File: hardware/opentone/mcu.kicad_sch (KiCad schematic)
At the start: 31 parts, among them J401 SWD 2x5 1.27mm, J402 ST-LINK (Nucleo CN4), J403 Log UART4, J404 Spare GPIO, SW401 RESET, SW402 BOOT0 (DFU), U401 STM32F446VETx, Y401 8MHz, Y402 32.768kHz

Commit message: added sd card, haptic, updated old parts and set a datasheet and MPN to all parts
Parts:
- C401, C402, C403, C404, C405, C406, C408, C410, C417: footprint Capacitor_SMD:C_0805_2012Metric -> Capacitor_SMD:C_0603_1608Metric; LCSC (none) -> C14663; Manufacturer (none) -> YAGEO; Part number (none) -> CC0603KRX7R9BB104
- C407: footprint Capacitor_SMD:C_0805_2012Metric -> Capacitor_SMD:C_0603_1608Metric; LCSC (none) -> C19666; Manufacturer (none) -> Samsung Electro-Mechanics; Part number (none) -> CL10A475KO8NNNC
- C409: footprint Capacitor_SMD:C_0805_2012Metric -> Capacitor_SMD:C_0603_1608Metric; LCSC (none) -> C15849; Manufacturer (none) -> Samsung Electro-Mechanics; Part number (none) -> CL10A105KB8NNNC
- C411, C412: footprint Capacitor_SMD:C_0805_2012Metric -> Capacitor_SMD:C_0603_1608Metric; LCSC (none) -> C23630; Manufacturer (none) -> Samsung Electro-Mechanics; Part number (none) -> CL10A225KO8NNNC
- C413, C414: footprint Capacitor_SMD:C_0805_2012Metric -> Capacitor_SMD:C_0603_1608Metric; LCSC (none) -> C1644; Manufacturer (none) -> Samsung Electro-Mechanics; Part number (none) -> CL10C150JB8NNNC
- C415, C416: footprint Capacitor_SMD:C_0805_2012Metric -> Capacitor_SMD:C_0603_1608Metric; LCSC (none) -> C1679; Manufacturer (none) -> FH (Guangdong Fenghua); Part number (none) -> 0603CG6R8C500NT
- FB401: footprint Inductor_SMD:L_0805_2012Metric -> Inductor_SMD:L_0603_1608Metric; LCSC (none) -> C1002; Manufacturer (none) -> Sunlord; Part number (none) -> GZ1608D601TF
- J401: LCSC (none) -> C150517; Manufacturer (none) -> Amphenol ICC; Part number (none) -> 20021121-00010C4LF; now left out of the parts list
- J402, J403, J404, JP401: now left out of the parts list
- R401: footprint Resistor_SMD:R_0805_2012Metric -> Resistor_SMD:R_0603_1608Metric; LCSC (none) -> C25804; Manufacturer (none) -> UNI-ROYAL; Part number (none) -> 0603WAF1002T5E
- R402, R403: footprint Resistor_SMD:R_0805_2012Metric -> Resistor_SMD:R_0603_1608Metric; LCSC (none) -> C23162; Manufacturer (none) -> UNI-ROYAL; Part number (none) -> 0603WAF4701T5E
- SW401, SW402: LCSC (none) -> C221895; Manufacturer (none) -> C&K; Part number (none) -> PTS810SJG250SMTRLFS
- U401: LCSC (none) -> C91929
- Y401: LCSC (none) -> C19076848; Manufacturer (none) -> KYX; Part number (none) -> K3A080001010
- Y402: LCSC (none) -> C20340322; Manufacturer (none) -> Seiko Epson; Part number (none) -> FC-135 32.7680KA-E

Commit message: added recommendations from Teel s checklists
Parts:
- added D401: STATUS, LED_SMD:LED_0603_1608Metric, symbol Device:LED
- added R404: 1k, Resistor_SMD:R_0603_1608Metric, symbol Device:R
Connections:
- net MCU_3V3: now also D401.2 (A)
- net SPARE_PC13 renamed STATUS_LED
- net STATUS_LED: now also R404.2
- new net: D401.1 (K), R404.1

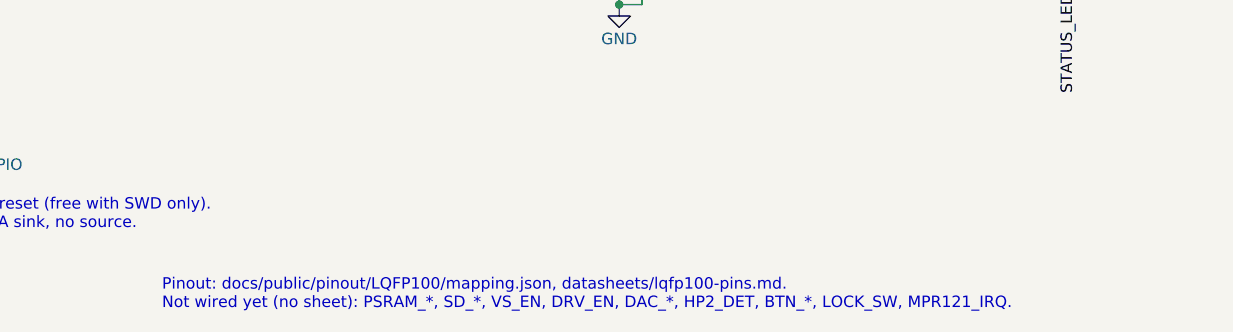
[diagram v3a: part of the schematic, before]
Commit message: license and datasheets script
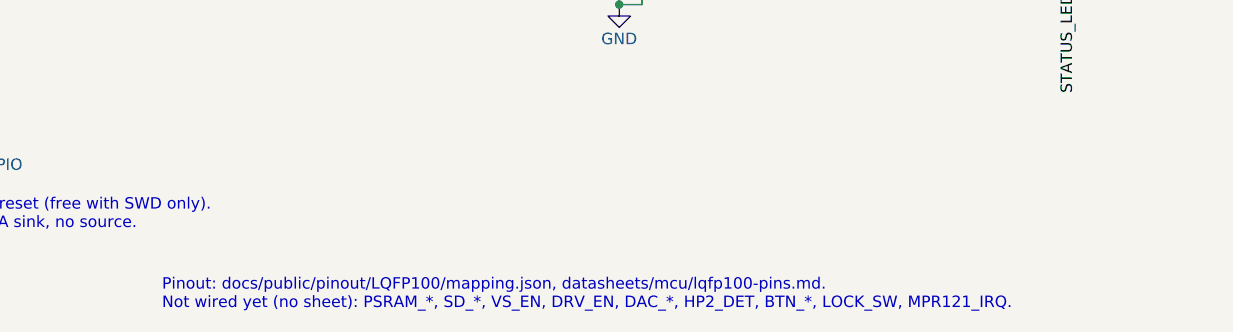
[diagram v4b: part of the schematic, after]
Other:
- note added: "Pinout: docs/public/pinout/LQFP100/mapping.json, datasheets/mcu/lqfp100-pins.md. Not wired yet (no sheet): PSRAM_*, SD_*, VS_EN, DRV_EN, DAC_*, HP2_DET, BTN_*, LOCK_SW, MPR121_IRQ."
- note removed: "Pinout: docs/public/pinout/LQFP100/mapping.json, datasheets/lqfp100-pins.md. Not wired yet (no sheet): PSRAM_*, SD_*, VS_EN, DRV_EN, DAC_*, HP2_DET, BTN_*, LOCK_SW, MPR121_IRQ."
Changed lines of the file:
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@@
 		(comment 1 "STM32F446VET6 (LQFP100), supply, crystals, reset/boot, SWD")
 	)
-	(text "Pinout: docs/public/pinout/LQFP100/mapping.json, datasheets/lqfp100-pins.md.\nNot wired yet (no sheet): PSRAM_*, SD_*, VS_EN, DRV_EN, DAC_*, HP2_DET, BTN_*, LOCK_SW, MPR121_IRQ."
+	(text "Pinout: docs/public/pinout/LQFP100/mapping.json, datasheets/mcu/lqfp100-pins.md.\nNot wired yet (no sheet): PSRAM_*, SD_*, VS_EN, DRV_EN, DAC_*, HP2_DET, BTN_*, LOCK_SW, MPR121_IRQ."
 		(exclude_from_sim no)
 		(at 177.8 248.92 0)

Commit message: DAC
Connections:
- net HP2_DET renamed DAC_INT

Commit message: updated BOM
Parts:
- C401, C402, C403, C404, C405, C406, C408, C410, C417: value 100n -> 100nF
- C407: value 4.7u -> 4.7uF
- C409: value 1u -> 1uF
- C411, C412: value 2.2u -> 2.2uF
- C413, C414: value 15p -> 15pF
- C415, C416: value 6.8p -> 6.8pF
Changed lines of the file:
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@@
 			)
 		)
-		(property "Value" "2.2u"
+		(property "Value" "2.2uF"
 			(at 92.71 71.12 0)
 			(show_name no)
@@
 			)
 		)
-		(property "Value" "1u"
+		(property "Value" "1uF"
 			(at 49.53 71.12 0)
 			(show_name no)
@@
 			)
 		)
-		(property "Value" "6.8p"
+		(property "Value" "6.8pF"
 			(at 120.65 104.14 0)
 			(show_name no)
@@
 			)
 		)
-		(property "Value" "100n"
+		(property "Value" "100nF"
 			(at 85.09 40.64 0)
 			(show_name no)
@@
 			)
 		)
-		(property "Value" "100n"
+		(property "Value" "100nF"
 			(at 59.69 71.12 0)
 			(show_name no)
@@
 			)
 		)
-		(property "Value" "100n"
+		(property "Value" "100nF"
 			(at 105.41 40.64 0)
 			(show_name no)
@@
 			)
 		)
-		(property "Value" "100n"
+		(property "Value" "100nF"
 			(at 54.61 40.64 0)
 			(show_name no)
@@
 			)
 		)
-		(property "Value" "100n"
+		(property "Value" "100nF"
 			(at 95.25 40.64 0)
 			(show_name no)
@@
 			)
 		)
-		(property "Value" "100n"
+		(property "Value" "100nF"
 			(at 64.77 40.64 0)
 			(show_name no)
@@
 			)
 		)
-		(property "Value" "100n"
+		(property "Value" "100nF"
 			(at 74.93 40.64 0)
 			(show_name no)
@@
 			)
 		)
-		(property "Value" "100n"
+		(property "Value" "100nF"
 			(at 125.73 40.64 0)
 			(show_name no)
@@
 			)
 		)
-		(property "Value" "15p"
+		(property "Value" "15pF"
 			(at 52.07 104.14 0)
 			(show_name no)
@@
 			)
 		)
-		(property "Value" "4.7u"
+		(property "Value" "4.7uF"
 			(at 115.57 40.64 0)
 			(show_name no)
@@
 			)
 		)
-		(property "Value" "100n"
+		(property "Value" "100nF"
 			(at 34.29 142.24 0)
 			(show_name no)
@@
 			)
 		)
-		(property "Value" "6.8p"
+		(property "Value" "6.8pF"
 			(at 95.25 104.14 0)
 			(show_name no)
@@
 			)
 		)
-		(property "Value" "2.2u"
+		(property "Value" "2.2uF"
 			(at 110.49 71.12 0)
 			(show_name no)
@@
 			)
 		)
-		(property "Value" "15p"
+		(property "Value" "15pF"
 			(at 26.67 104.14 0)
 			(show_name no)

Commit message: started placing the components
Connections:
- net SPARE_PA2 renamed IQS_RDY
- net USB_DM renamed USB_DN
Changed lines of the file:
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@@
-		)
-	)
-	(label "SPARE_PA2"
-		(at 259.08 86.36 0)
-		(effects
-			(font
-				(size 1.27 1.27)
-			)
-			(justify left bottom)
 		)
 	)
@@
 		)
 	)
-	(label "SPARE_PA2"
-		(at 142.24 215.9 180)
-		(effects
-			(font
-				(size 1.27 1.27)
-			)
-			(justify right bottom)
-		)
-	)
 	(label "SWCLK"
 		(at 259.08 116.84 0)
@@
 		)
 	)
-	(global_label "USB_DM"
+	(global_label "USB_DN"
 		(shape bidirectional)
 		(at 259.08 109.22 0)
@@
 		)
 	)
+	(global_label "IQS_RDY"
+		(shape input)
+		(at 259.08 86.36 0)
+		(fields_autoplaced yes)
+		(effects
+			(font
+				(size 1.27 1.27)
+			)
+			(justify left)
+		)
+		(property "Intersheetrefs" "${INTERSHEET_REFS}"
+			(at 259.08 86.36 0)
+			(hide yes)
+			(show_name no)
+			(do_not_autoplace no)
+			(effects
+				(font
+					(size 1.27 1.27)
+				)
+				(justify left)
+			)
+		)
+	)
 	(global_label "NRST"
 		(shape bidirectional)
@@
 			(hide yes)
 			(show_name no)
+			(do_not_autoplace no)
+			(effects
+				(font
+					(size 1.27 1.27)
+				)
+				(justify right)
+			)
+		)
+	)
+	(global_label "IQS_RDY"
+		(shape input)
+		(at 142.24 215.9 180)
+		(fields_autoplaced yes)
+		(effects
+			(font
+				(size 1.27 1.27)
+			)
+			(justify right)
+		)
+		(property "Intersheetrefs" "${INTERSHEET_REFS}"
+			(at 142.24 215.9 180)
+			(hide yes)
+			(show_name no)
